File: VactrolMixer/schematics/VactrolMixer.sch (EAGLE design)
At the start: 67 parts, among them IC1 NE5532N, IC2 NE5532N, IC3 NE5532N, IC4 NE5532N, IC5 NE5532N, IC6 NE5532N, T1 2N3904, T2 2N3904, T3 2N3904, T4 2N3904

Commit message: tidied
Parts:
- removed IN_1: CON-LUMBERG_1502_03, Rebel:CON-LUMBERG_1502_03
- removed POT1A, POT1B: POT-ALPS_ALPS290024, Rebel:POT-ALPS_ALPS290024
- removed R19, R21: (no value), resistor:R-EU_0411/15
- removed R33: 33k, resistor:R-EU_0411/15
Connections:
- removed net N$26: IN_1.3, POT1A.2, POT1B.2
- removed net N$43: IN_1.4, R33.2
- removed net N$8: POT1B.3, R21.2
- net GND: no longer POT1A.1, POT1B.1
- net N$52: no longer R19.1
- net N$54: no longer R21.1
- net V+: no longer R33.1
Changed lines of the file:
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@@
 <part name="SUPPLY4" library="supply2" deviceset="V+" device=""/>
 <part name="GND16" library="supply1" deviceset="GND" device=""/>
-<part name="R19" library="resistor" deviceset="R-EU_" device="0411/15"/>
-<part name="POT1A" library="Rebel" deviceset="POT-ALPS_ALPS290024" device=""/>
-<part name="IN_1" library="Rebel" deviceset="CON-LUMBERG_1502_03" device=""/>
-<part name="R21" library="resistor" deviceset="R-EU_" device="0411/15"/>
-<part name="POT1B" library="Rebel" deviceset="POT-ALPS_ALPS290024" device=""/>
-<part name="GND11" library="supply1" deviceset="GND" device=""/>
-<part name="GND13" library="supply1" deviceset="GND" device=""/>
 <part name="U$1" library="Pingdynasty" deviceset="VTL5C3" device=""/>
 <part name="LED1" library="led" deviceset="LED" device="5MM"/>
@@
 <part name="R31" library="resistor" deviceset="R-EU_" device="0411/15" value="10k"/>
 <part name="SUPPLY5" library="supply2" deviceset="V+" device=""/>
-<part name="R33" library="resistor" deviceset="R-EU_" device="0411/15" value="33k"/>
-<part name="SUPPLY7" library="supply2" deviceset="V+" device=""/>
 <part name="R1" library="resistor" deviceset="R-EU_" device="0411/15"/>
 <part name="POT2A" library="Rebel" deviceset="POT-ALPS_ALPS290024" device=""/>
@@
 <text x="-76.2" y="-114.3" size="1.778" layer="97">Widlar Current Source</text>
 <text x="-124.46" y="-101.6" size="1.778" layer="97">Adding non-inverting amp</text>
+<wire x1="-78.74" y1="-5.08" x2="-43.18" y2="-5.08" width="0.1524" layer="97"/>
+<wire x1="-78.74" y1="-111.76" x2="-43.18" y2="-111.76" width="0.1524" layer="97"/>
 </plain>
 <instances>
@@
 <instance part="SUPPLY4" gate="1" x="-144.78" y="35.56"/>
 <instance part="GND16" gate="1" x="-144.78" y="7.62"/>
-<instance part="R19" gate="G$1" x="-116.84" y="93.98" rot="R90"/>
-<instance part="POT1A" gate="G$1" x="-116.84" y="109.22"/>
-<instance part="IN_1" gate="G$1" x="-104.14" y="124.46" rot="R90"/>
-<instance part="R21" gate="G$1" x="-116.84" y="45.72" rot="R90"/>
-<instance part="POT1B" gate="G$1" x="-116.84" y="60.96"/>
-<instance part="GND11" gate="1" x="-121.92" y="48.26"/>
-<instance part="GND13" gate="1" x="-121.92" y="96.52"/>
 <instance part="U$1" gate="G$1" x="5.08" y="-124.46"/>
 <instance part="LED1" gate="G$1" x="-17.78" y="-121.92" rot="R270"/>
@@
 <instance part="R31" gate="G$1" x="-165.1" y="22.86" rot="R90"/>
 <instance part="SUPPLY5" gate="1" x="-165.1" y="35.56"/>
-<instance part="R33" gate="G$1" x="-104.14" y="111.76" rot="R90"/>
-<instance part="SUPPLY7" gate="1" x="-96.52" y="114.3"/>
 <instance part="R1" gate="G$1" x="-81.28" y="93.98" rot="R90"/>
 <instance part="POT2A" gate="G$1" x="-81.28" y="109.22"/>
@@
 </segment>
 <segment>
-<wire x1="-121.92" y1="50.8" x2="-121.92" y2="55.88" width="0.1524" layer="91"/>
-<pinref part="GND11" gate="1" pin="GND"/>
-<pinref part="POT1B" gate="G$1" pin="1"/>
-</segment>
-<segment>
-<wire x1="-121.92" y1="99.06" x2="-121.92" y2="104.14" width="0.1524" layer="91"/>
-<pinref part="GND13" gate="1" pin="GND"/>
-<pinref part="POT1A" gate="G$1" pin="1"/>
-</segment>
-<segment>
 <wire x1="-71.12" y1="-149.86" x2="-71.12" y2="-162.56" width="0.1524" layer="91"/>
 <wire x1="-71.12" y1="-162.56" x2="-60.96" y2="-162.56" width="0.1524" layer="91"/>
@@
 <pinref part="SUPPLY1" gate="1" pin="V+"/>
 <pinref part="U$1" gate="G$1" pin="LED+"/>
-</segment>
-<segment>
-<wire x1="-96.52" y1="111.76" x2="-96.52" y2="104.14" width="0.1524" layer="91"/>
-<wire x1="-96.52" y1="104.14" x2="-104.14" y2="104.14" width="0.1524" layer="91"/>
-<wire x1="-104.14" y1="104.14" x2="-104.14" y2="106.68" width="0.1524" layer="91"/>
-<pinref part="SUPPLY7" gate="1" pin="V+"/>
-<pinref part="R33" gate="G$1" pin="1"/>
 </segment>
 <segment>
@@
 </segment>
 </net>
-<net name="N$26" class="0">
-<segment>
-<wire x1="-111.76" y1="53.34" x2="-111.76" y2="55.88" width="0.1524" layer="91"/>
-<wire x1="-111.76" y1="101.6" x2="-111.76" y2="104.14" width="0.1524" layer="91"/>
-<wire x1="-111.76" y1="101.6" x2="-106.68" y2="101.6" width="0.1524" layer="91"/>
-<wire x1="-106.68" y1="101.6" x2="-106.68" y2="119.38" width="0.1524" layer="91"/>
-<wire x1="-111.76" y1="53.34" x2="-106.68" y2="53.34" width="0.1524" layer="91"/>
-<wire x1="-106.68" y1="53.34" x2="-106.68" y2="101.6" width="0.1524" layer="91"/>
-<junction x="-106.68" y="101.6"/>
-<pinref part="POT1B" gate="G$1" pin="2"/>
-<pinref part="POT1A" gate="G$1" pin="2"/>
-<pinref part="IN_1" gate="G$1" pin="3"/>
-</segment>
-</net>
 <net name="N$15" class="0">
 <segment>
@@
 </segment>
 </net>
-<net name="N$43" class="0">
-<segment>
-<wire x1="-104.14" y1="116.84" x2="-104.14" y2="119.38" width="0.1524" layer="91"/>
-<pinref part="IN_1" gate="G$1" pin="4"/>
-<pinref part="R33" gate="G$1" pin="2"/>
-</segment>
-</net>
 <net name="N$11" class="0">
 <segment>
@@
 </segment>
 </net>
-<net name="N$8" class="0">
-<segment>
-<wire x1="-116.84" y1="50.8" x2="-116.84" y2="55.88" width="0.1524" layer="91"/>
-<pinref part="R21" gate="G$1" pin="2"/>
-<pinref part="POT1B" gate="G$1" pin="3"/>
-</segment>
-</net>
 <net name="N$52" class="0">
 <segment>
-<wire x1="-116.84" y1="88.9" x2="-116.84" y2="83.82" width="0.1524" layer="91"/>
 <wire x1="-81.28" y1="88.9" x2="-81.28" y2="83.82" width="0.1524" layer="91"/>
-<wire x1="-116.84" y1="83.82" x2="-81.28" y2="83.82" width="0.1524" layer="91"/>
 <wire x1="-48.26" y1="88.9" x2="-48.26" y2="83.82" width="0.1524" layer="91"/>
 <wire x1="-81.28" y1="83.82" x2="-48.26" y2="83.82" width="0.1524" layer="91"/>
@@
 <wire x1="60.96" y1="83.82" x2="60.96" y2="76.2" width="0.1524" layer="91"/>
 <wire x1="-12.7" y1="83.82" x2="60.96" y2="83.82" width="0.1524" layer="91"/>
-<junction x="-81.28" y="83.82"/>
 <junction x="-48.26" y="83.82"/>
 <junction x="-12.7" y="83.82"/>
 <junction x="60.96" y="83.82"/>
-<pinref part="R19" gate="G$1" pin="1"/>
 <pinref part="R1" gate="G$1" pin="1"/>
 <pinref part="R5" gate="G$1" pin="1"/>
@@
 <net name="N$54" class="0">
 <segment>
-<wire x1="-116.84" y1="35.56" x2="-116.84" y2="40.64" width="0.1524" layer="91"/>
 <wire x1="-81.28" y1="35.56" x2="-81.28" y2="40.64" width="0.1524" layer="91"/>
-<wire x1="-116.84" y1="35.56" x2="-81.28" y2="35.56" width="0.1524" layer="91"/>
 <wire x1="-48.26" y1="35.56" x2="-48.26" y2="40.64" width="0.1524" layer="91"/>
 <wire x1="-81.28" y1="35.56" x2="-48.26" y2="35.56" width="0.1524" layer="91"/>
@@
 <wire x1="66.04" y1="27.94" x2="60.96" y2="27.94" width="0.1524" layer="91"/>
 <wire x1="-12.7" y1="35.56" x2="60.96" y2="35.56" width="0.1524" layer="91"/>
-<junction x="-81.28" y="35.56"/>
 <junction x="-48.26" y="35.56"/>
 <junction x="-12.7" y="35.56"/>
 <junction x="60.96" y="35.56"/>
-<pinref part="R21" gate="G$1" pin="1"/>
 <pinref part="R3" gate="G$1" pin="1"/>
 <pinref part="R9" gate="G$1" pin="1"/>
@@
 <net name="N$18" class="0">
 <segment>
+<pinref part="POTA" gate="G$1" pin="3"/>
+<wire x1="-147.32" y1="-12.7" x2="-147.32" y2="-17.78" width="0.1524" layer="91"/>
 <pinref part="R45" gate="G$1" pin="2"/>
-<pinref part="POTA" gate="G$1" pin="3"/>
-<wire x1="-127" y1="-12.7" x2="-147.32" y2="-12.7" width="0.1524" layer="91"/>
-<wire x1="-147.32" y1="-12.7" x2="-147.32" y2="-17.78" width="0.1524" layer="91"/>
-</segment>
-</net>
-<net name="N$23" class="0">
-<segment>
-<pinref part="CV_A" gate="G$1" pin="3"/>
-<pinref part="POTA" gate="G$1" pin="2"/>
-<wire x1="-185.42" y1="-12.7" x2="-152.4" y2="-12.7" width="0.1524" layer="91"/>
-<wire x1="-152.4" y1="-12.7" x2="-152.4" y2="-17.78" width="0.1524" layer="91"/>
+<wire x1="-147.32" y1="-12.7" x2="-127" y2="-12.7" width="0.1524" layer="91"/>
 </segment>
 </net>
@@
 </segment>
 </net>
+<net name="N$7" class="0">
+<segment>
+<pinref part="CV_A" gate="G$1" pin="3"/>
+<pinref part="POTA" gate="G$1" pin="2"/>
+<wire x1="-185.42" y1="-12.7" x2="-152.4" y2="-12.7" width="0.1524" layer="91"/>
+<wire x1="-152.4" y1="-12.7" x2="-152.4" y2="-17.78" width="0.1524" layer="91"/>
+</segment>
+</net>

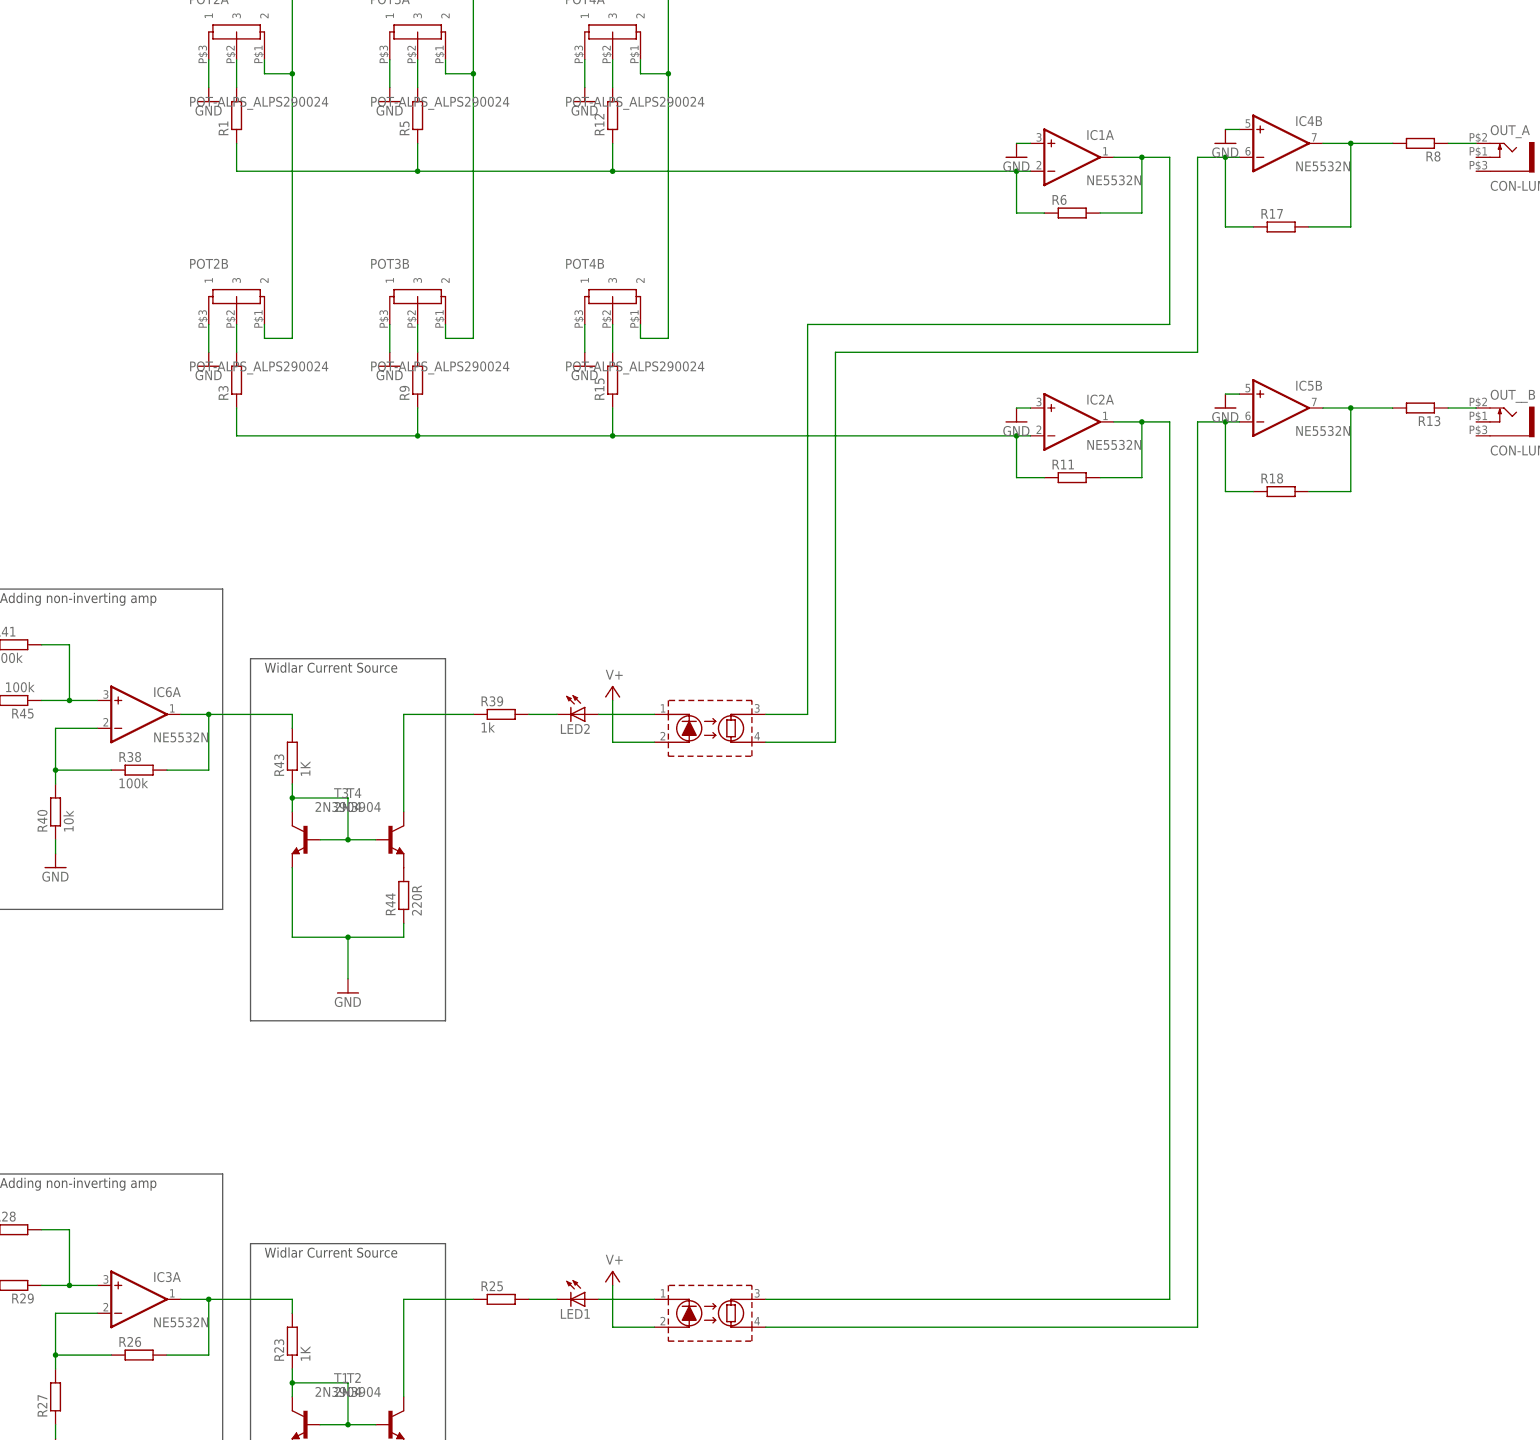
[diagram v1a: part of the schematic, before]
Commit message: set values, invoked op amps
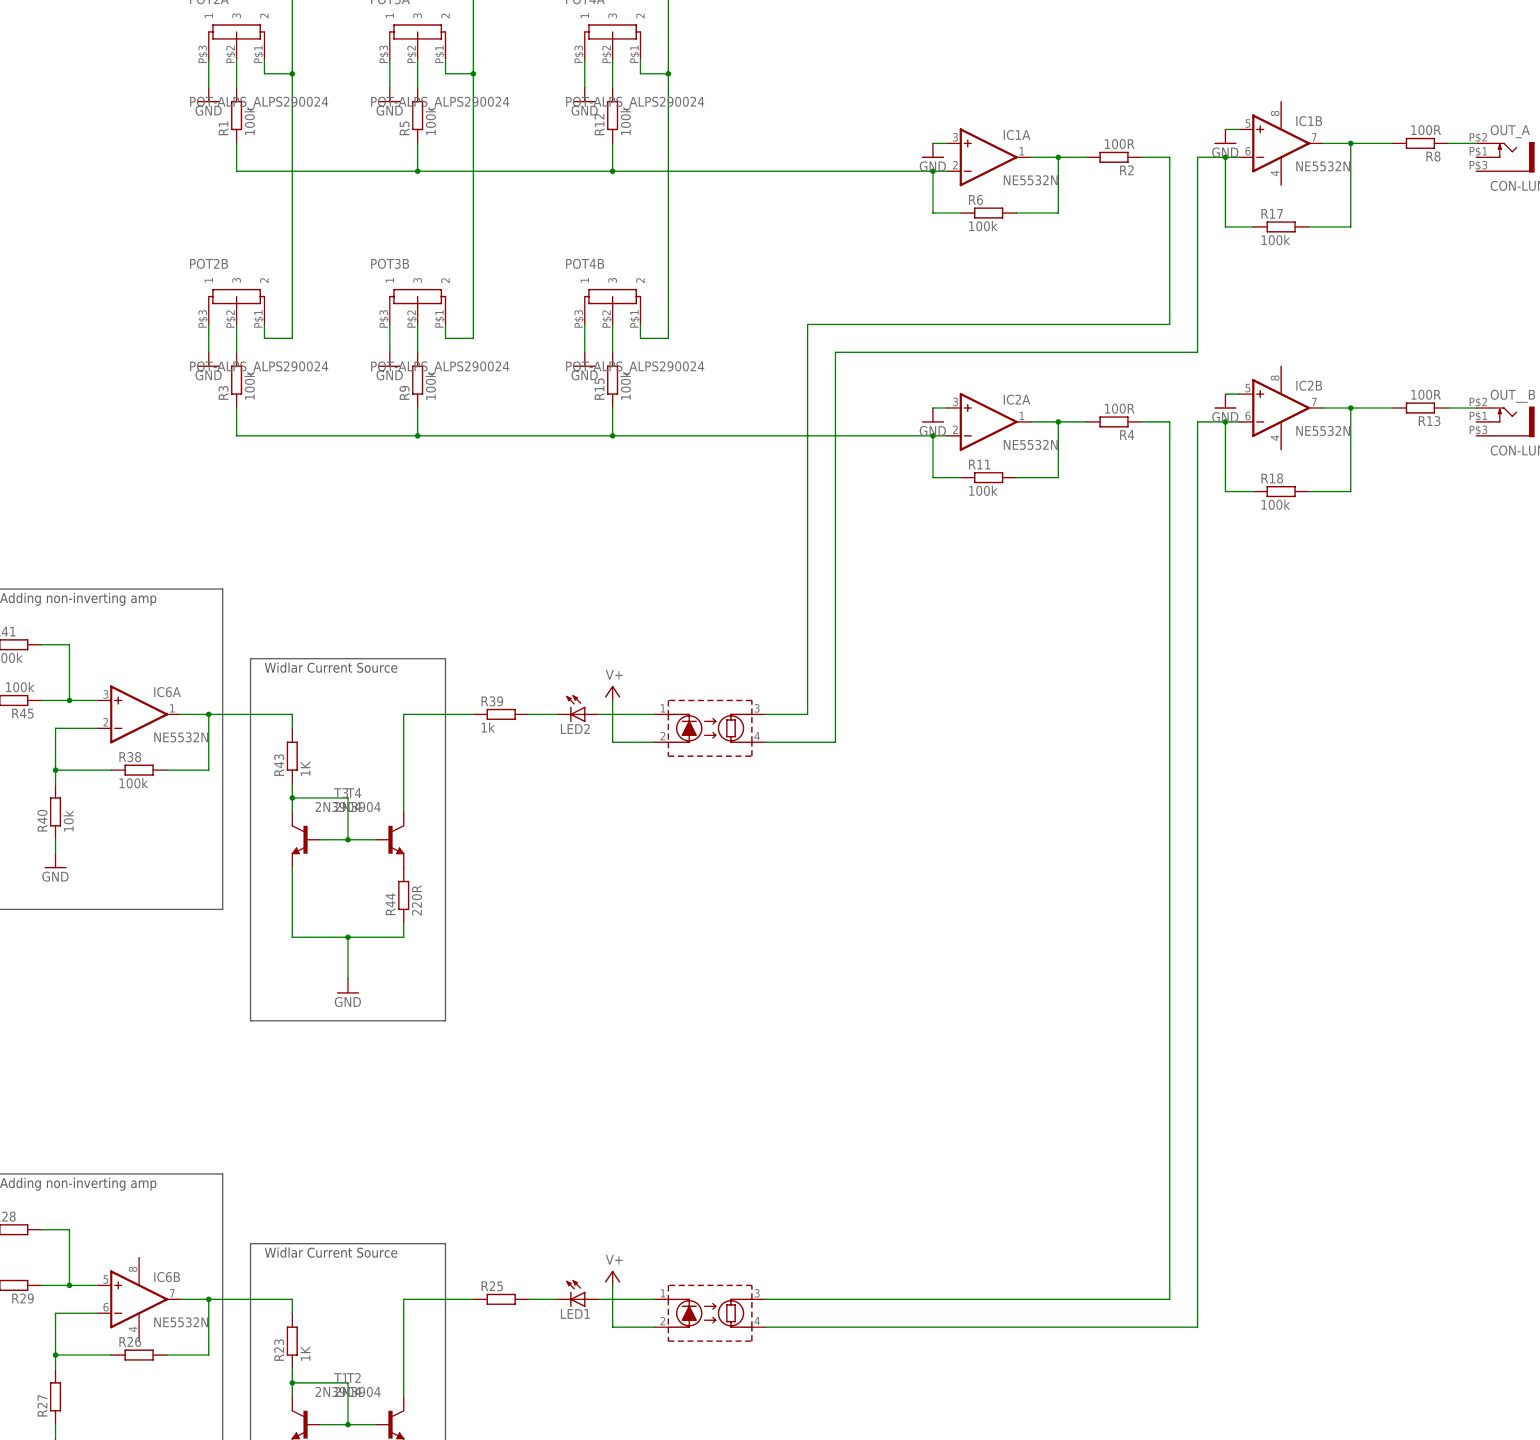
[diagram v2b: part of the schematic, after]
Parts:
- removed IC3, IC4, IC5: NE5532N, linear:NE5532N
- added R2, R4: 100R, resistor:R-EU_0411/15
- LED1, LED2: device led:LED5MM -> Rebel:LED3MM
- R1, R11, R12, R15, R17, R18, R3, R5, R6, R9: value (none) -> 100k
- R13, R8: value (none) -> 100R
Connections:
- new net N$8: IC1A.OUT, R2.2, R6.2
- new net N$9: IC2A.OUT, R11.2, R4.2
- net GND: now also IC1B.+IN, IC2B.+IN; no longer IC4B.+IN, IC5B.+IN
- net N$1: now also IC1B.OUT; no longer IC4B.OUT
- net N$11: now also IC1B.-IN; no longer IC4B.-IN
- net N$14: now also IC2B.OUT; no longer IC5B.OUT
- net N$17: now also IC6B.OUT; no longer IC3A.OUT
- net N$3: now also R4.1; no longer IC2A.OUT, R11.2
- net N$30: now also IC6B.-IN; no longer IC3A.-IN
- net N$32: now also IC6B.+IN; no longer IC3A.+IN
- net N$36: now also IC2B.-IN; no longer IC5B.-IN
- net N$4: now also R2.1; no longer IC1A.OUT, R6.2
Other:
- moved on the sheet: IC1A, IC2A, R11, R6

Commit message: added output files
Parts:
- removed R39: 1k, resistor:R-EU_0411/15
- R17, R18: value 100k -> 20k
- R36, R42: value 10k -> 2k2
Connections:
- removed net N$24: CV_A.4, R31.1, R36.2
- removed net N$41: R39.1, T3.C
- removed net N$47: CV_B.4, R32.1, R42.2
- new net N$20: R31.1, R36.2, R45.2
- new net N$23: R29.2, R32.1, R42.2
- net N$18: now also R31.2; no longer R45.2
- net N$37: now also R32.2; no longer R29.2
- net N$40: now also T3.C; no longer R39.2
- net V+: now also CV_A.4, CV_B.4; no longer R31.2, R32.2
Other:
- moved on the sheet: POTA, POTB, R31, R32, R36, R42

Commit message: added power input, added back 4th input, changed power supply
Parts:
- added C1, C2, C3: (no value), SparkFun:CAPPTH2
- added C4, C5: 10u, rcl:CPOL-EUE5-6
- added D1, D2, D3: (no value), Rebel:DIODE1N4001
- added F1, F2, F3: PTCPTH, Rebel:PTCPTH
- added IN_1: CON-LUMBERG_1502_03, Rebel:CON-LUMBERG_1502_03
- added POT1A, POT1B: POT-ALPS_ALPS290024, Rebel:POT-ALPS_ALPS290024
- added R10, R7: 100k, resistor:R-EU_0411/15
- added U$3: M08X2, SparkFun:M08X2
- renumbered CV_A to CV_MA, CV_B to CV_MB, POTA to POTMA, POTB to POTMB
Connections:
- removed net N$52: IC1A.-IN, R1.1, R12.1, R5.1, R6.1
- removed net V+: CV_MA.4, CV_MB.4, R34.E, R35.E, U$1.LED+, U$2.LED+
- new net +12V: C1.1, C2.1, C3.1, C4.+, CV_MA.4, CV_MB.4, D2.C, F2.2, IC1P.V+, IC2P.V+, IC6P.V+, R34.E, R35.E, U$1.LED+, U$2.LED+
- new net +5V: D1.C, F1.2
- new net -12V: C1.2, C2.2, C3.2, C5.-, D3.A, F3.1, IC1P.V-, IC2P.V-, IC6P.V-
- new net N$24: IC1A.-IN, R1.1, R12.1, R5.1, R6.1, R7.1
- new net N$26: IC2A.-IN, R10.1, R11.1, R15.1, R3.1, R9.1
- new net N$33: IN_1.3, POT1A.2, POT1B.2
- new net N$41: IN_1.4
- new net N$43: POT1A.3, R7.2
- new net N$47: POT1B.3, R10.2
- new net N$55: F1.1, U$3.11, U$3.12
- new net N$56: F2.1, U$3.10, U$3.9
- new net N$57: F3.2, U$3.1, U$3.2
- new net PWR_BUS: U$3.15, U$3.16
- net GND: now also C4.-, C5.+, D1.A, D2.A, D3.C, POT1A.1, POT1B.1, U$3.3, U$3.4, U$3.5, U$3.6, U$3.7, U$3.8
- net N$54: now also U$3.13, U$3.14; no longer IC2A.-IN, R11.1, R15.1, R3.1, R9.1
